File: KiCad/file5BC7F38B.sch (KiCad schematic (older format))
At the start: 74 parts, among them J301 DB9_Female, P301 ISP/PDI, P302 Thru, P304 Header, SW301 Sync, U301 DS3231, U302 ATmega1284P-AU, U304 SI5351A, U305 74HC1G08, U306 MIC5219-3.3BM5, U307 SN74CB3Q3305, U308 MIC5219-3.3BM5, X301 ASTX-H11-25.MHZ, Y301 20 MHz

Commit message: Design Updates
Specifying components
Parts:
- removed C311: 100nF, Capacitors_SMD:C_0805_HandSoldering, symbol Device:C
- removed C? (x2): 100nF, Capacitors_SMD:C_0805_HandSoldering, symbol Device:C_Small
- removed C?: 2.2uF, Capacitors_SMD:C_0805_HandSoldering, symbol Device:C
- removed D302: 1.7V, Diodes_SMD:SOD-123_Handsolder, symbol FlexFox80-rescue:ZENER-ARDF-2-Band-MiniTx-rescue
- removed D303: MBD54DWT1G_Schottky_Ind, TO_SOT_Packages_SMD:SOT-363_Handsolder, symbol FlexFox80-rescue:MBD54DWT1G_Schottky_Ind-ARDF-2-Band-MiniTx-rescue
- removed R? (x2): 10k, Resistors_SMD:R_0805_HandSoldering, symbol Device:R
- removed R?: 100k, Resistors_SMD:R_0805_HandSoldering, symbol Device:R
- added C311, C319, C320: 100nF, Capacitors_SMD:C_0805, symbol Device:C_Small
- added C318: 4.7uF, Capacitors_SMD:C_0805_HandSoldering, symbol Device:C
- added unit 2 of D301
- added R303, R311: 10k, Resistors_SMD:R_0805, symbol Device:R
- added R308: 100k, Resistors_SMD:R_0805_HandSoldering, symbol Device:R
- BT301: Description (none) -> BATTERY HOLDER COIN 12MM SMD; Digi-Key Part No. (none) -> BC501SM-ND; Manufacturer (none) -> MPD (Memory Protection Devices); Manufacturer PN (none) -> BC501SM; Part No. BC501SM-ND -> (none)
- C302, C306, C307, C308, C309, C316: footprint Capacitors_SMD:C_0805_HandSoldering -> Capacitors_SMD:C_0805; Description (none) -> CAP CER 0.1UF 50V X7R 0805; Digi-Key Part No. (none) -> 478-1395-1-ND; Manufacturer (none) -> AVX Corporation; Manufacturer PN (none) -> 08055C104KAT2A; Part No. 478-1395-1-ND -> (none)
- C303: renamed from C?; value 2.2uF -> 4.7uF; Description (none) -> CAP CER 4.7UF 25V X7R 0805; Digi-Key Part No. (none) -> 587-2990-1-ND; Link <a href=\"https://www.digikey.com/products/en?keywords=1276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 -> <a href=\"https://www.digikey.com/products/en?keywords=587-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; Manufacturer (none) -> Taiyo Yuden; Manufacturer PN (none) -> TMK212AB7475KG-T; Part No. 1276-1763-1-ND -> (none)
- C305: footprint Capacitors_SMD:C_0805_HandSoldering -> Capacitors_SMD:C_0805; Description (none) -> CAP CER 10UF 25V X5R 0805; Digi-Key Part No. (none) -> 490-5523-1-ND; Manufacturer (none) -> Murata Electronics; Manufacturer PN (none) -> GRM21BR61E106KA73L; Part No. 490-5523-1-ND -> (none)
- C313, C314, C315, C317: value 2.2uF -> 4.7uF; Description (none) -> CAP CER 4.7UF 25V X7R 0805; Digi-Key Part No. (none) -> 587-2990-1-ND; Link <a href=\"https://www.digikey.com/products/en?keywords=1276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 -> <a href=\"https://www.digikey.com/products/en?keywords=587-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; Manufacturer (none) -> Taiyo Yuden; Manufacturer PN (none) -> TMK212AB7475KG-T; Part No. 1276-1763-1-ND -> (none)
- D301: renamed from D?; Digi-Key Part No. (none) -> MBD54DWT1GOSCT-ND; Part No. MBD54DWT1GOSCT-ND -> (none)
- D304: footprint (none) -> Resistors_SMD:R_0805; Description (none) -> LED GREEN CLEAR 0805 SMD; Digi-Key Part No. (none) -> 732-4983-1-ND; Link (none) -> <a href=\"https://www.digikey.com/products/en?keywords=732-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; Manufacturer (none) -> Wurth Elektronik; Manufacturer PN (none) -> 150080GS75000
- D305: footprint (none) -> Resistors_SMD:R_0805; Description (none) -> LED RED CLEAR 0805 SMD; Digi-Key Part No. (none) -> 732-4984-1-ND; Link (none) -> <a href=\"https://www.digikey.com/products/en?keywords=732-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; Manufacturer (none) -> Wurth Elektronik; Manufacturer PN (none) -> 150080RS75000
- J301: footprint (none) -> Connect:DB9F_CI; Description (none) -> CONN D-SUB RCPT 9POS SLDR CUP; Digi-Key Part No. (none) -> 609-1525-ND; Link (none) -> <a href=\"https://www.digikey.com/products/en?keywords=609-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; Manufacturer (none) -> Amphenol ICC (FCI); Manufacturer PN (none) -> DE09S064TLF
- MOD301: Digi-Key Part No. (none) -> 1528-1223-ND; Part No. 1528-1223-ND -> (none)
- P301: Digi-Key Part No. (none) -> 609-3487-1-ND; Part No. 609-3487-1-ND -> (none)
- Q301: renamed from Q?; footprint Package_TO_SOT_THT:TO-92_Inline -> TO_SOT_Packages_SMD:SOT-23; Description (none) -> TRANS NPN 40V 0.6A SOT23; Digi-Key Part No. (none) -> MMBT2222ATPMSCT-ND; Link (none) -> <a href=\"https://www.digikey.com/products/en?keywords=MMBT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; Manufacturer (none) -> Micro Commercial Co; Manufacturer PN (none) -> MMBT2222A-TP
- R301, R302: footprint Resistors_SMD:R_0805_HandSoldering -> Resistors_SMD:R_0805; Description (none) -> RES 470 OHM 1% 1/4W 0805; Digi-Key Part No. (none) -> 2019-RK73H2ATTD4700FCT-ND; Link <a href=\"https://www.digikey.com/products/en?keywords=311-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 -> <a href=\"https://www.digikey.com/products/en?keywords=2019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; Manufacturer (none) -> KOA Speer Electronics, Inc.; Manufacturer PN (none) -> RK73H2ATTD4700F; Part No. 311-10.0KCRCT-ND -> (none)
- R304: footprint Resistors_SMD:R_0805_HandSoldering -> Resistors_SMD:R_0805; Description (none) -> RES SMD 10 OHM 1% 1/8W 0805; Digi-Key Part No. (none) -> 311-10.0CRCT-ND; Manufacturer (none) -> Yageo; Manufacturer PN (none) -> RC0805FR-0710RL; Part No. 311-10.0CRCT-ND -> (none)
- R305, R306, R307, R310: footprint Resistors_SMD:R_0805_HandSoldering -> Resistors_SMD:R_0805; Description (none) -> RES SMD 10K OHM 1% 1/8W 0805; Digi-Key Part No. (none) -> 311-10KLGCT-ND; Link <a href=\"https://www.digikey.com/products/en?keywords=311-10.0KCRCT-ND\">Link</a> -> <a href=\"https://www.digikey.com/products/en?keywords=311-10KLGCT-ND\">Link</a>; Manufacturer (none) -> Yageo; Manufacturer PN (none) -> AC0805FR-0710KL; Part No. 311-10.0KCRCT-ND -> (none)
- R309: renamed from R?; footprint Resistors_SMD:R_0805_HandSoldering -> Resistors_SMD:R_0805; Description (none) -> RES SMD 2.2K OHM 1% 1/8W 0805; Digi-Key Part No. (none) -> 311-2.2KCRCT-ND; Manufacturer (none) -> Yageo; Manufacturer PN (none) -> RC0805FR-072K2L; Part No. 311-10.0KCRCT-ND -> (none)
- R312: renamed from R?; value 1M -> 560k; footprint Resistors_SMD:R_0805_HandSoldering -> Resistors_SMD:R_0805; Description (none) -> RES SMD 560K OHM 1% 1/8W 0805; Digi-Key Part No. (none) -> 13-RT0805FRE07560KLCT-ND; Link <a href=\"https://www.digikey.com/products/en?keywords=311-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 -> <a href=\"https://www.digikey.com/products/en?keywords=13-R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; Manufacturer (none) -> Yageo; Manufacturer PN (none) -> RT0805FRE07560KL; Part No. 311-10.0KCRCT-ND -> (none)
- R313: renamed from R?; Description (none) -> RES SMD 10K OHM 1% 1/8W 0805; Digi-Key Part No. (none) -> 311-100KCRCT-ND; Link <a href=\"https://www.digikey.com/products/en?keywords=311-10.0KCRCT-ND\">Link</a> -> <a href=\"https://www.digikey.com/products/en?keywords=311-100KCRCT-ND\">Link</a>; Manufacturer (none) -> Yageo; Manufacturer PN (none) -> RC0805FR-07100KL; Part No. 311-10.0KCRCT-ND -> (none)
- RV301: renamed from RV?; value R_POT -> 10k Pot; footprint (none) -> Potentiometers:Potentiometer_ST32ET_Handsolder; Description (none) -> TRIMMER 10K OHM 0.1W J LEAD TOP; Digi-Key Part No. (none) -> TC33X-103ECT-ND; Link (none) -> <a href=\"https://www.digikey.com/products/en?keywords=TC33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; Manufacturer (none) -> Bourns Inc.; Manufacturer PN (none) -> TC33X-2-103E
- SW301: value Sync -> SPST; footprint (none) -> Buttons_Switches_SMD:PTS645SL50SMTR92; Description (none) -> SWITCH TACTILE SPST-NO 0.05A 12V; Digi-Key Part No. (none) -> CKN9088CT-ND; Link (none) -> <a href=\"https://www.digikey.com/products/en?keywords=CKN9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; Manufacturer (none) -> C&K; Manufacturer PN (none) -> PTS645SL50SMTR92 LFS
- U301: footprint SMD_Packages:SO16_Handsolder -> SMD_Packages:SO16; Description (none) -> IC RTC CLK/CALENDAR I2C 16-SOIC; Digi-Key Part No. (none) -> DS3231S#T&RCT-ND; Manufacturer (none) -> Maxim Integrated; Manufacturer PN (none) -> DS3231S#T&R; Part No. DS3231S#T&RCT-ND -> (none)
- U302: Description (none) -> IC MCU 8BIT 128KB FLASH 44TQFP; Digi-Key Part No. (none) -> ATMEGA1284P-AU-ND; Link (none) -> <a href=\"https://www.digikey.com/products/en?keywords=ATME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; Manufacturer (none) -> Microchip Technology; Manufacturer PN (none) -> ATMEGA1284P-AU
- U303: renamed from U?; value MIC5219-3.3BM5 -> LP2992; footprint TO_SOT_Packages_SMD:SOT-23-5_Handsolder -> TO_SOT_Packages_SMD:SOT-23-5; Description (none) -> IC REG LINEAR 3.3V 250MA SOT23-5; Digi-Key Part No. (none) -> LP2992AIM5-3.3/NOPBCT-ND; Link <a href=\"https://www.digikey.com/products/en?keywords=576-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 -> <a href=\"https://www.digikey.com/products/en?keywords=LP29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; Manufacturer (none) -> Texas Instruments; Manufacturer PN (none) -> LP2992AIM5-3.3/NOPB; Part No. 576-1281-1-ND -> (none)
- U304: Digi-Key Part No. (none) -> 336-2399-5-ND; Part No. 336-2399-5-ND -> (none)
- U305: footprint TO_SOT_Packages_SMD:SOT-23-5_Handsolder -> TO_SOT_Packages_SMD:SOT-23-5; symbol FlexFox80-rescue:74HC1G08-ARDF-2-Band-MiniTx-rescue -> 74xx:74HC1G08; Description (none) -> IC GATE AND 1CH 2-INP 5TSOP; Digi-Key Part No. (none) -> MC74HC1G08DTT1GOSCT-ND; Manufacturer (none) -> ON Semiconductor; Manufacturer PN (none) -> MC74HC1G08DTT1G; Part No. MC74HC1G08DTT1GOSCT-ND -> (none)
- U306, U308: value MIC5219-3.3BM5 -> LP2992; footprint TO_SOT_Packages_SMD:SOT-23-5_Handsolder -> TO_SOT_Packages_SMD:SOT-23-5; Description (none) -> IC REG LINEAR 3.3V 250MA SOT23-5; Digi-Key Part No. (none) -> LP2992AIM5-3.3/NOPBCT-ND; Link <a href=\"https://www.digikey.com/products/en?keywords=576-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 -> <a href=\"https://www.digikey.com/products/en?keywords=LP29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; Manufacturer (none) -> Texas Instruments; Manufacturer PN (none) -> LP2992AIM5-3.3/NOPB; Part No. 576-1281-1-ND -> (none)
- U307: Digi-Key Part No. (none) -> 296-16809-1-ND; Part No. 296-16809-1-ND -> (none)
- X301: Digi-Key Part No. (none) -> 535-12039-1-ND; Part No. 535-12039-1-ND -> (none)
- gave numbers to parts that had none: 3
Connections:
- net +12V: now also U306.5 (VOUT); no longer U306.1 (VIN)
- net +3V3_L8: now also C316.2, C311.2, C318.2; no longer C316.1
- net 3V3_PWR_ENABLE: now also R303.2
- net EXTERNAL_3.2V-12V_SUPPLY: now also C314.2, U308.1 (VIN), U308.3 (EN)
- net GND: now also C302.1, C306.1, C316.1, C311.1, C318.1, R303.1; no longer C302.2, C306.2, C316.2
- net MOSI: now also R308.1
- net PROC_HT_AUDIO_IN: now also C320.1
- net PROC_PTT_OUT: now also R311.2
- net Vproc: now also C302.2, C306.2, D301.6 (C), R305.2, D301.3 (C); no longer C302.1, C306.1, D301.3 (C), R305.1
- net WIFI_ENABLE: now also U306.4 (BYP); no longer U306.3 (EN)
- net ~RESET~: now also R305.1, D301.4 (A); no longer R305.2
- net at C313.2, MOD301.9 (VBat): now also U306.1 (VIN); no longer U306.5 (VOUT)
- net at J301.5: now also C320.2
- net at Q301.1 (B): now also R311.1
- net at RV301.1: now also R308.2
- net at RV301.2: now also C319.1
- net at J301.1, R309.2: now also C319.2
- net at J301.7: now also D301.1 (A); no longer D301.4 (A)

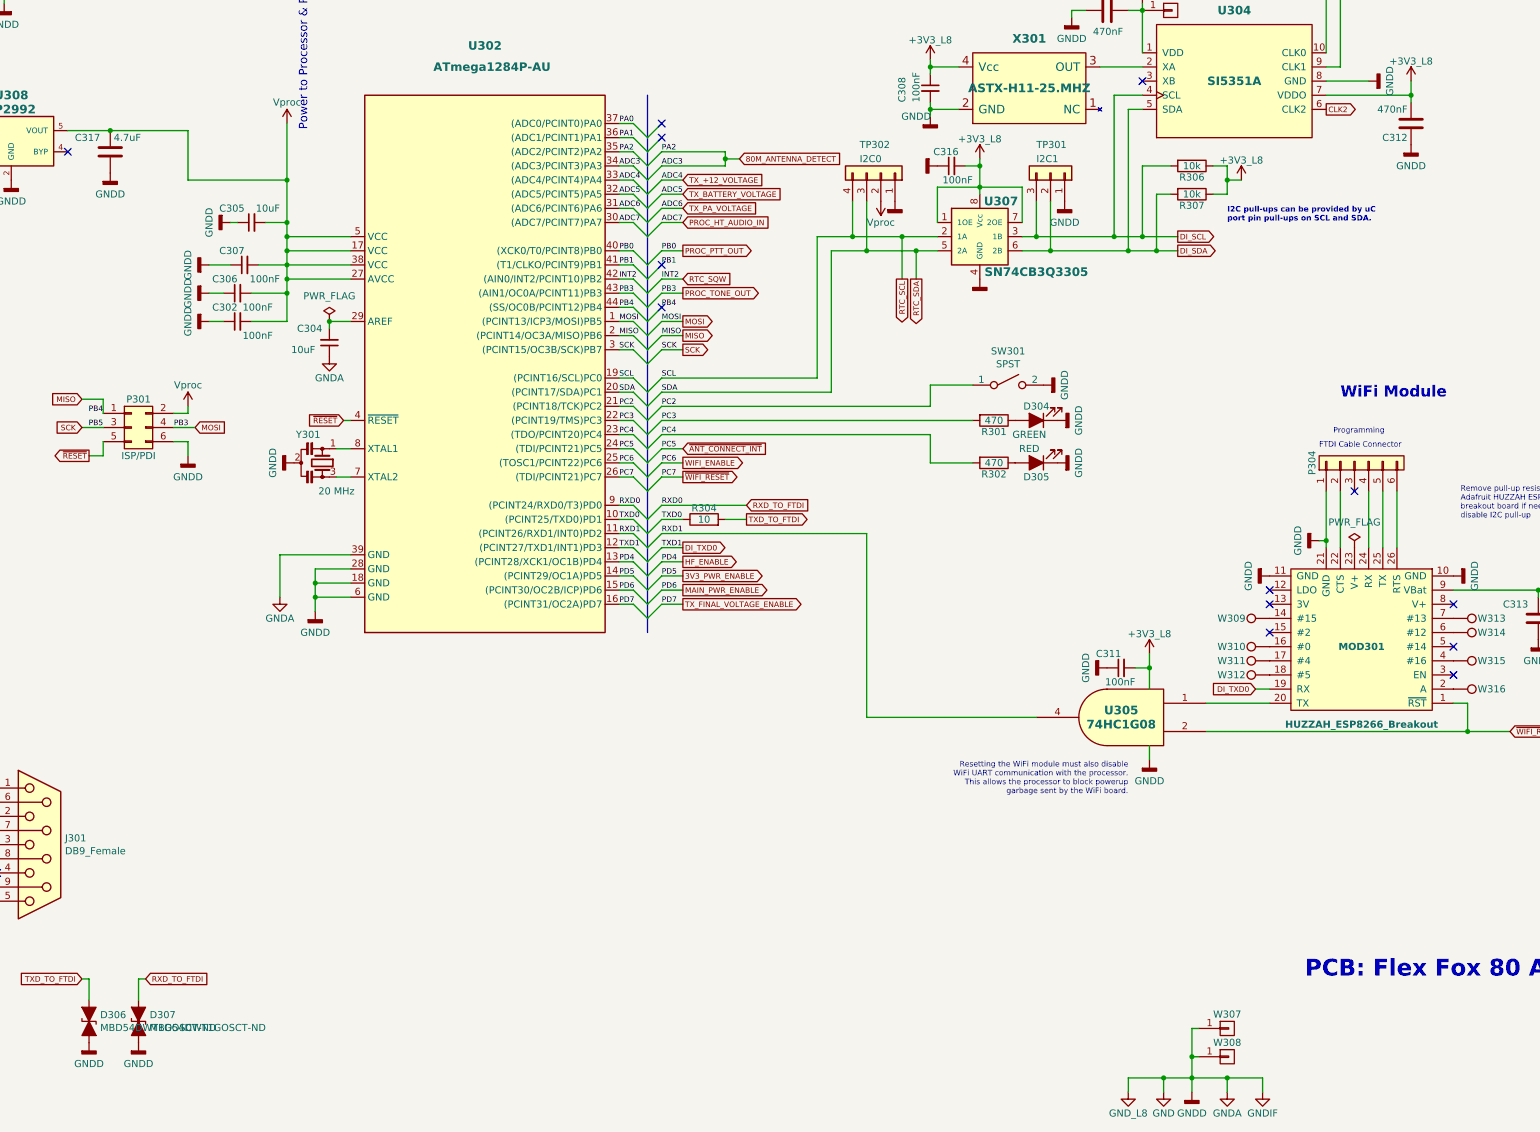
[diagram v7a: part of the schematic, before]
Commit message: Design Updates
Defining parts and footprints
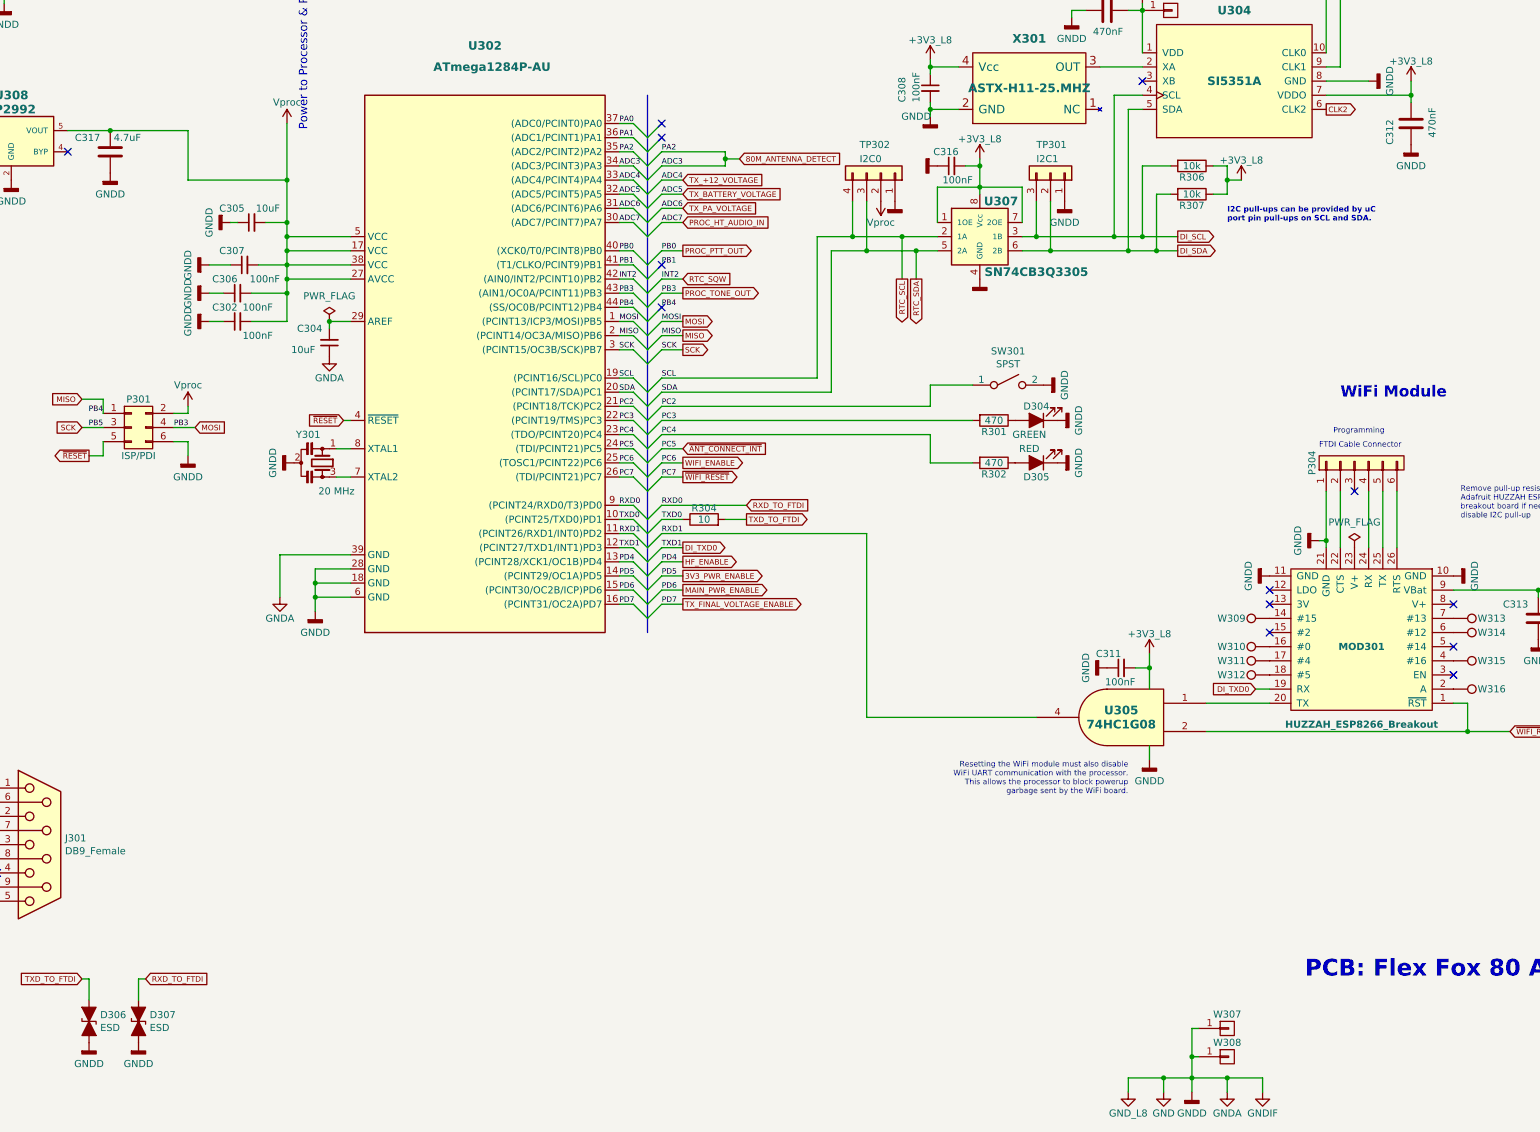
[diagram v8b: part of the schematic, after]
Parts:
- C301: footprint Capacitors_SMD:C_0805_HandSoldering -> Capacitors_SMD:C_0805; Description (none) -> CAP CER 1UF 16V X7R 0805; Digi-Key Part No. (none) -> 311-1365-1-ND; Manufacturer (none) -> Yageo; Manufacturer PN (none) -> CC0805KKX7R7BB105; Part No. 311-1365-1-ND -> (none)
- C304: Description (none) -> CAP CER 10UF 25V X5R 0805; Digi-Key Part No. (none) -> 490-5523-1-ND; Manufacturer (none) -> Murata Electronics; Manufacturer PN (none) -> GRM21BR61E106KA73L; Part No. 490-5523-1-ND -> (none)
- C310, C312: footprint Capacitors_SMD:C_0805_HandSoldering -> Capacitors_SMD:C_0805; Description (none) -> CAP CER 0.47UF 100V X7R 0805; Digi-Key Part No. (none) -> 478-9924-1-ND; Manufacturer (none) -> AVX Corporation; Manufacturer PN (none) -> 08051C474K4Z2A; Part No. 478-9924-1-ND -> (none)
- D306, D307: value MBD54DWT1GOSCT-ND -> ESD; footprint TO_SOT_Packages_SMD:SOT-363-0.65 -> Resistors_SMD:R_0603; Description (none) -> VARISTOR 0603; Digi-Key Part No. (none) -> CG0603MLC-05LECT-ND; Link (none) -> <a href=\"https://www.digikey.com/products/en?keywords=CG06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; Manufacturer (none) -> Bourns Inc.; Manufacturer PN (none) -> CG0603MLC-05LE
- MOD301: Description (none) -> ESP8266 HUZZAH BREAKOUT BOARD; Manufacturer (none) -> Adafruit Industries LLC; Manufacturer PN (none) -> 2471
- P301: Description (none) -> CONN HEADER SMD 6POS 2.54MM; Manufacturer (none) -> Amphenol ICC (FCI); Manufacturer PN (none) -> 95278-101A06LF
- P304, W307, W308: Digi-Key Part No. (none) -> np; Manufacturer (none) -> np; Part No. np -> (none)
- TP301, TP302: Digi-Key Part No. (none) -> np; Link (none) -> np; Manufacturer (none) -> np
- U304: Description (none) -> IC CLK GENERATOR 200MHZ 10MSOP; Manufacturer (none) -> Silicon Labs; Manufacturer PN (none) -> SI5351A-B-GT
- U307: Description (none) -> IC BUS SWITCH 1 X 1:1 8TSSOP; Manufacturer (none) -> Texas Instruments; Manufacturer PN (none) -> SN74CB3Q3305PWR
- X301: footprint Crystals:ASTX-H11 -> Crystals:ASTX-H11-25.000MHZ; Description (none) -> XTAL OSC TCXO 25.0000MHZ HCMOS; Manufacturer (none) -> Abracon LLC; Manufacturer PN (none) -> ASTX-H11-25.000MHZ-T
- Y301: footprint (none) -> Crystals:CSTNE20M0V53Z000R0; Description (none) -> CERAMIC RES 20.0000MHZ 15PF SMD; Digi-Key Part No. (none) -> 490-17955-1-ND; Link (none) -> <a href=\"https://www.digikey.com/products/en?keywords=490-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; Manufacturer (none) -> Murata Electronics; Manufacturer PN (none) -> CSTNE20M0V53Z000R0; Part No. CSTNE20M0V53Z000R0 -> (none)
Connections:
- net +3V3_L8: now also C312.1; no longer C312.2
- net GND: now also C312.2; no longer C312.1
